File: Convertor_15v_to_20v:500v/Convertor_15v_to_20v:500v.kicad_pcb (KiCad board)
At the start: 2 copper layers, 90 x 80 mm, 54 parts, among them J1 Screw_Terminal_01x04, J2 Conn_01x04_Male, Q1 IRF640NSTR, T1 Transfomer_1P_1S_custom, U1 OP177, U10 CPC1977, U2 UC3845_DIP8, U3 DCP011515D, U4 ISO124P, U5 DCP011515D, U6 CPC1977, U7 CPC1977, U8 PVN012, U9 CPC1977

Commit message: tester up
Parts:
- removed the U5 at (169.2, 145.0)
- added PS1: TMV1215D, Converter_DCDC:Converter_DCDC_XP_POWER-IHxxxxSH_THT, F.Cu at (162.8, 142.0)
- D2: value 1.5KE75A -> 1.5K100A
- L1: value L -> 4uH
- R10: value 30k 1% -> 36k 1%
- moved C9 10.8 mm to (163.2, 146.8), turned to 0 degrees
- moved C14 9.68 mm to (173.6, 145.0)
- moved C13 3.68 mm to (177.6, 145.0)
- renumbered C8 to C10, C9 to C11, C11 to C12, C14 to C13, C12 to C14, C6 to C5, C5 to C6, C10 to C7, C7 to C8, C13 to C9, R18 to R17, U6 to U5, U7 to U6, U8 to U7, U9 to U8, U10 to U9
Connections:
- C13 pad 1: Net-(C14-Pad1) -> Net-(C13-Pad1)
- C14 pad 1: +15V -> Net-(C14-Pad1)
- C14 pad 2: GND -> GND2
- C9 pad 1: Net-(C13-Pad1) -> +15V
- C9 pad 2: GND2 -> GND
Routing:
- net GND2: track 132.1 -> 116.8 mm
- net Net-(C13-Pad1): track 23.3 -> 18.5 mm
- net Net-(C14-Pad1): track 20.7 -> 16.5 mm
- net +15V: track 117.1 -> 119.6 mm

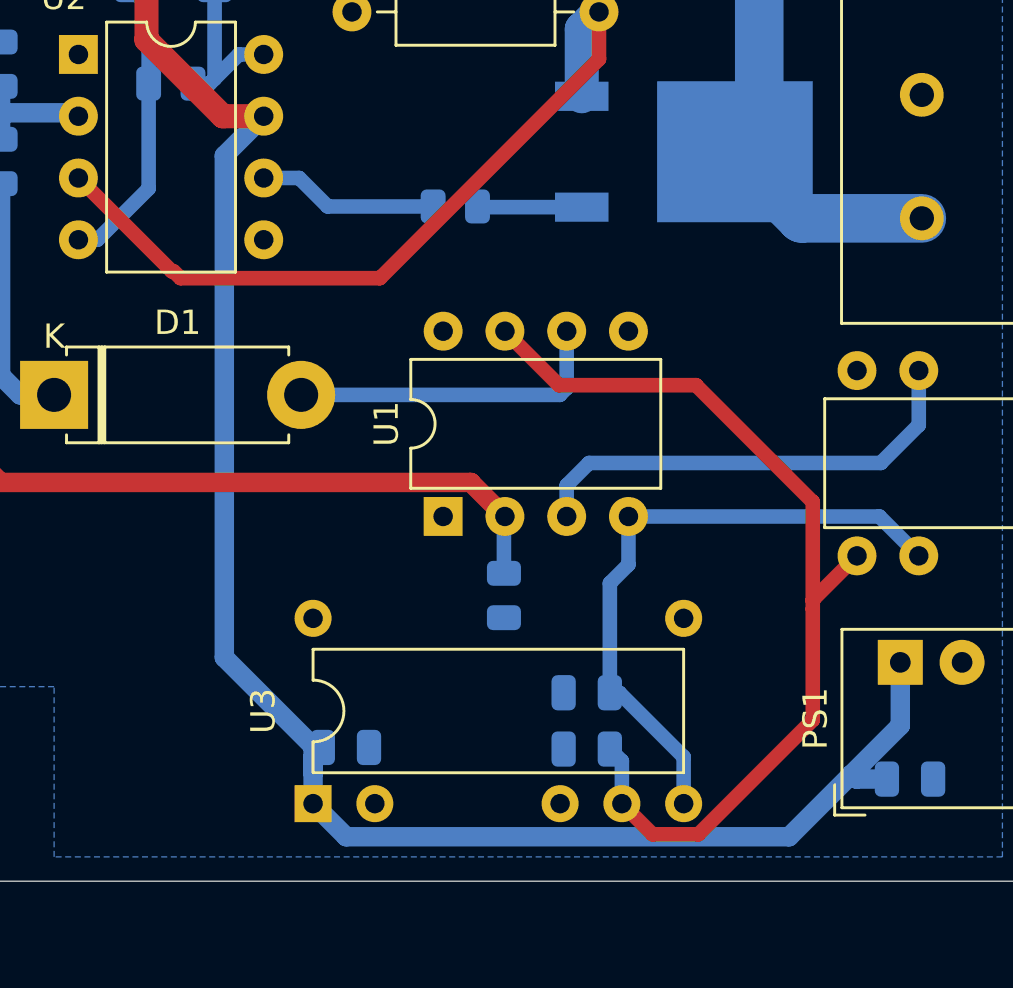
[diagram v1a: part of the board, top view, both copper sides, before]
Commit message: Convertor edit dcp011515 to tmv1215d
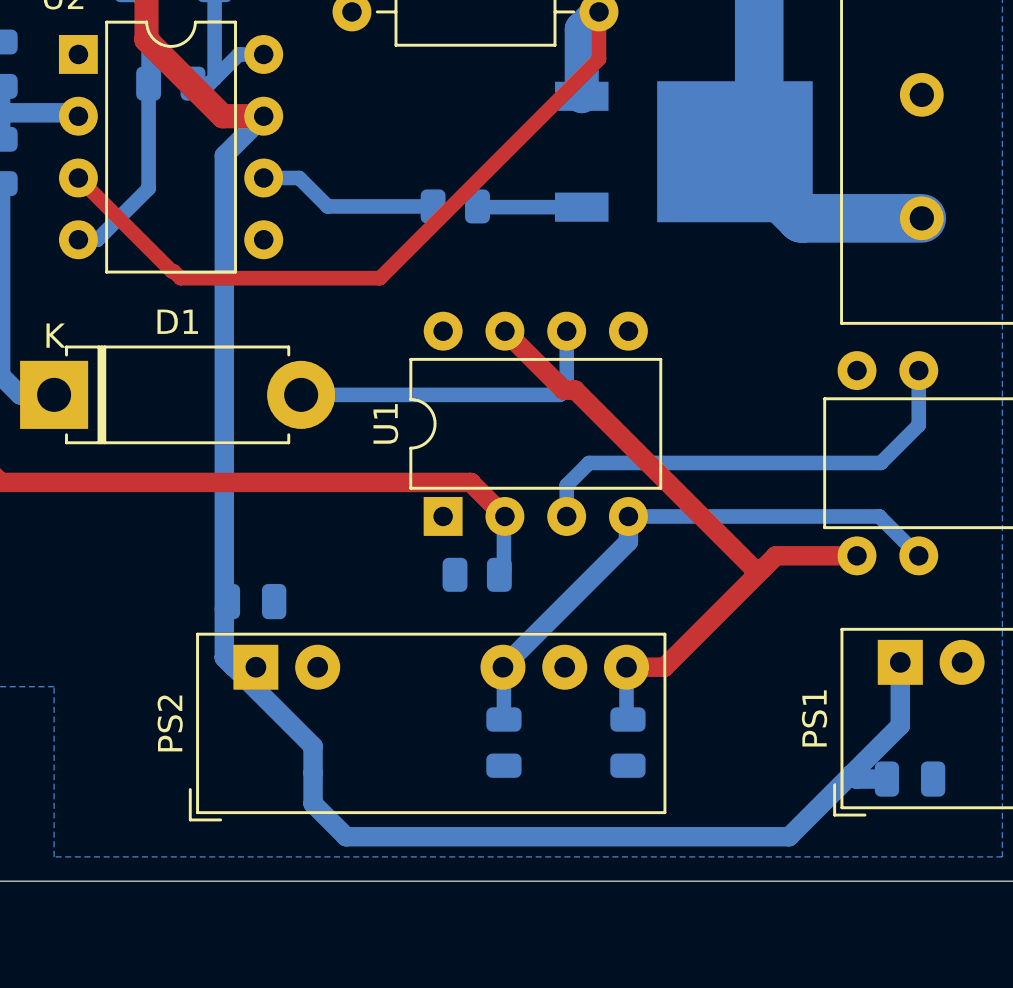
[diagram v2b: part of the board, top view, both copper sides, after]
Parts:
- removed U3: DCP011515D, Converter_DCDC:Converter_DCDC_DCP01xxxxD
- added PS2: TMV1215D, Converter_DCDC:Converter_DCDC_XP_POWER-IHxxxxSH_THT, F.Cu at (136.3, 142.2)
- R7: value 0.2 -> 0.2 0.25W
- U2: value UC3845_DIP8 -> UC3845
- moved C5 7.16 mm to (136.1, 139.5)
- moved C7 3.97 mm to (146.5, 145.3), turned to 270 degrees
- moved C8 1.72 mm to (151.6, 145.3), turned to 270 degrees
- moved R4 1.39 mm to (145.4, 138.4), turned to 0 degrees
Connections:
- net +15V renamed +12V
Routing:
- net Net-(C8-Pad1): track 39.9 -> 28.2 mm
- net Net-(C7-Pad1): track 26.2 -> 23.1 mm
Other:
- board text added: "+12V"
- board text removed: "+15V"
